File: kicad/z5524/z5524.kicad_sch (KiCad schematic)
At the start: 46 parts, among them J2 Conn_01x01, J3 Conn_02x20_Odd_Even, J4 Conn_01x02, Q2 MMBT3904, U10 LM337L_TO92, U11 PCA9555D, U13 DG442xY, U14 TL072, U19 LM4040BIM3-4.1, U20 M24C02-WMN, U5 LM4040C25FTA, U8 TL074, U9 LM78L05_TO92

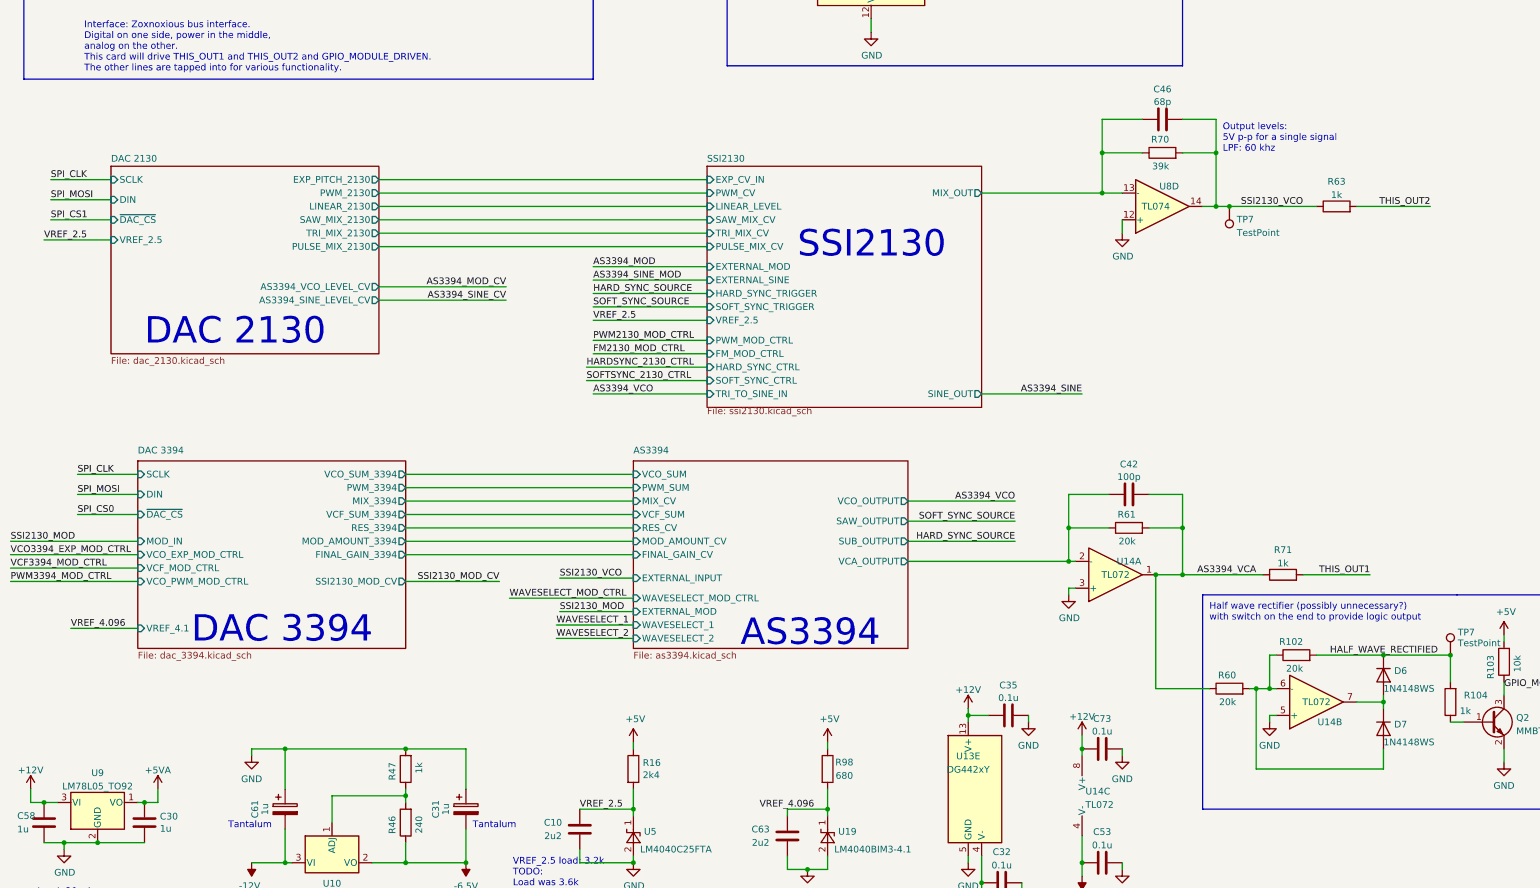
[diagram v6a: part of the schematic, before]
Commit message: updates to scale modulation values better
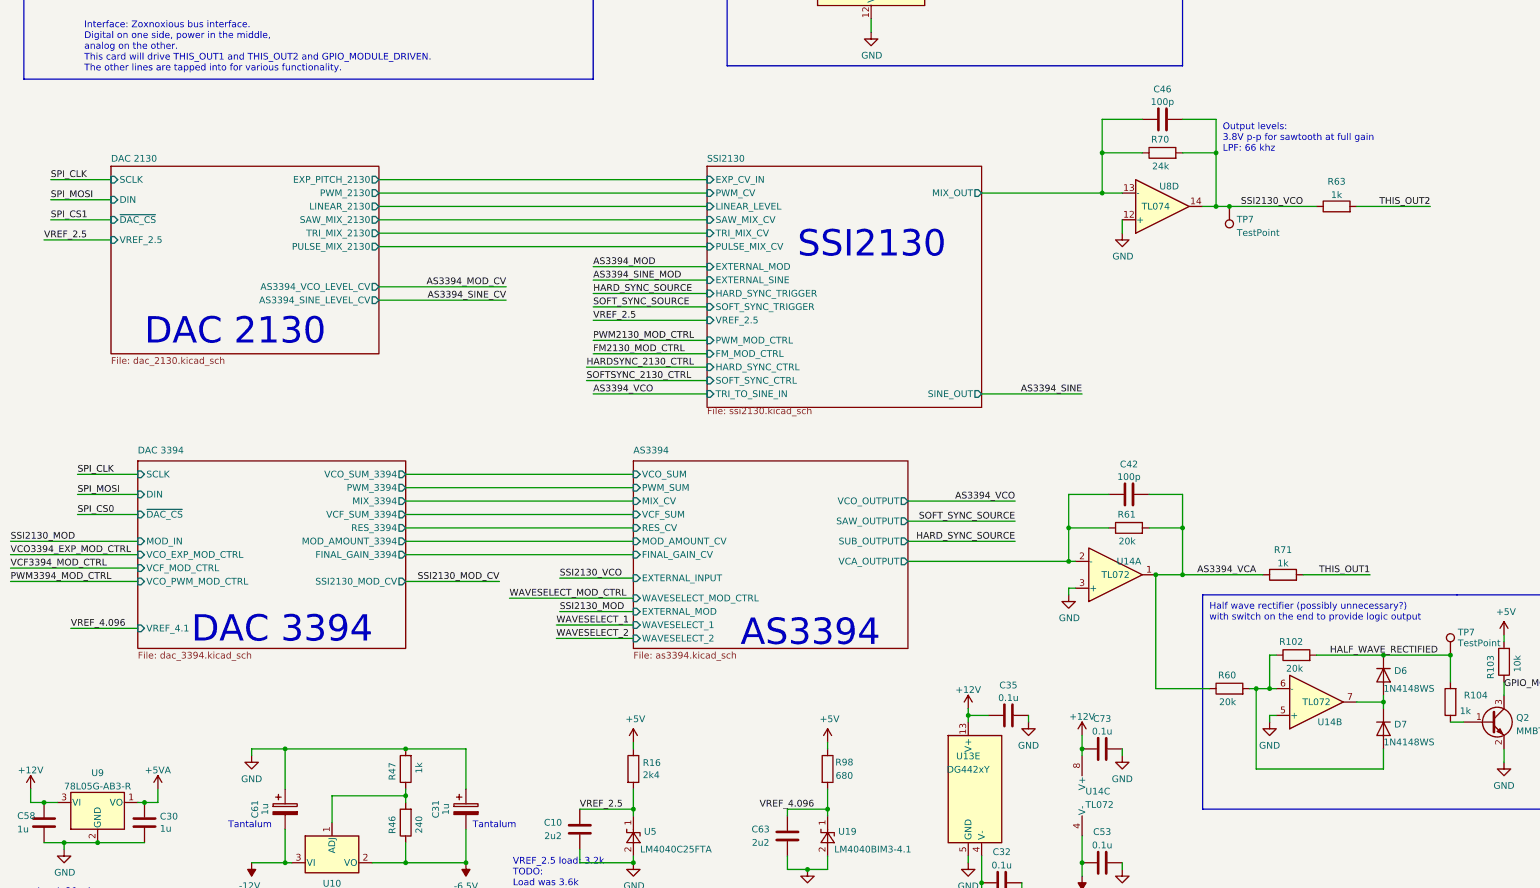
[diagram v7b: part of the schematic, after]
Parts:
- C46: value 68p -> 100p; LCSC C28262 -> C14858
- R70: value 39k -> 24k; LCSC C23153 -> C23352
- U9: value LM78L05_TO92 -> 78L05G-AB3-R; footprint Package_TO_SOT_THT:TO-92_Inline_Wide -> Package_TO_SOT_SMD:SOT-89-3; LCSC (none) -> C71136
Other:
- note added: "Output levels: 3.8V p-p for sawtooth at full gain LPF: 66 khz"
- note removed: "Output levels: 5V p-p for a single signal LPF: 60 khz"
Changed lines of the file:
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@@
     (effects (font (size 1.27 1.27)) (justify left bottom))
   )
-  (text "Output levels:\n5V p-p for a single signal\nLPF: 60 khz"
+  (text "Output levels:\n3.8V p-p for sawtooth at full gain\nLPF: 66 khz"
     (at 243.84 118.11 0)
     (effects (font (size 1.27 1.27)) (justify left bottom))
@@
       (effects (font (size 1.27 1.27)) (justify left))
     )
-    (property "Value" "39k" (at 233.68 120.65 90)
+    (property "Value" "24k" (at 233.68 120.65 90)
       (effects (font (size 1.27 1.27)) (justify left))
     )
@@
       (effects (font (size 1.27 1.27)) hide)
     )
-    (property "LCSC" "C23153" (at 232.41 118.11 0)
+    (property "LCSC" "C23352" (at 232.41 118.11 0)
       (effects (font (size 1.27 1.27)) hide)
     )
@@
       (effects (font (size 1.27 1.27)))
     )
-    (property "Value" "LM78L05_TO92" (at 30.48 238.2321 0)
-      (effects (font (size 1.27 1.27)))
-    )
-    (property "Footprint" "Package_TO_SOT_THT:TO-92_Inline_Wide" (at 30.48 235.585 0)
+    (property "Value" "78L05G-AB3-R" (at 30.48 238.2321 0)
+      (effects (font (size 1.27 1.27)))
+    )
+    (property "Footprint" "Package_TO_SOT_SMD:SOT-89-3" (at 30.48 235.585 0)
       (effects (font (size 1.27 1.27) italic) hide)
     )
-    (property "Datasheet" "https://www.onsemi.com/pub/Collateral/MC78L06A-D.pdf" (at 30.48 242.57 0)
+    (property "Datasheet" "https://datasheet.lcsc.com/lcsc/2304140030_UTC-Unisonic-Tech-78L05G-AB3-R_C71136.pdf" (at 30.48 242.57 0)
+      (effects (font (size 1.27 1.27)) hide)
+    )
+    (property "LCSC" "C71136" (at 30.48 241.3 0)
       (effects (font (size 1.27 1.27)) hide)
     )
@@
       (effects (font (size 1.27 1.27)))
     )
-    (property "Value" "68p" (at 232.41 108.4381 90)
+    (property "Value" "100p" (at 232.41 108.4381 90)
       (effects (font (size 1.27 1.27)))
     )
@@
       (effects (font (size 1.27 1.27)) hide)
     )
-    (property "LCSC" "C28262" (at 232.41 111.76 0)
-      (effects (font (size 1.27 1.27)) hide)
-    )
+    (property "LCSC" "C14858" (at 232.41 111.76 0)
+      (effects (font (size 1.27 1.27)) hide)
+    )

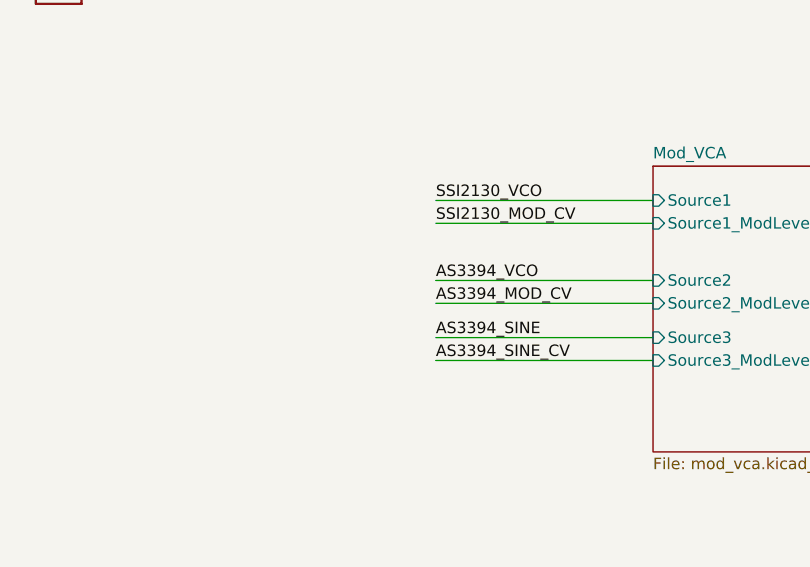
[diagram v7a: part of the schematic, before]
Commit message: schematic updates- cv values from dac and input protections between VCOs
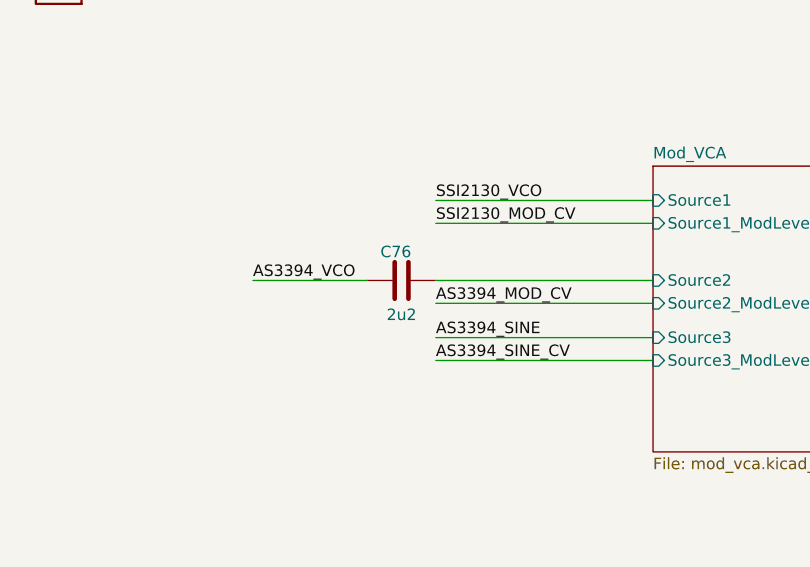
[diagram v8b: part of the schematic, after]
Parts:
- added C76: 2u2, Capacitor_SMD:C_0603_1608Metric, symbol Device:C
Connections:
- net AS3394_VCO: now also C76.2
- new net Mod_VCA/Source2: C76.1
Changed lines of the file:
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@@
+    (stroke (width 0) (type default))
+  )
+  (wire (pts (xy 287.02 160.02) (xy 299.72 160.02))
     (stroke (width 0) (type default))
   )
@@
     (effects (font (size 1.27 1.27)) (justify right bottom))
   )
-  (label "AS3394_VCO" (at 307.34 160.02 0) (fields_autoplaced)
+  (label "AS3394_VCO" (at 287.02 160.02 0) (fields_autoplaced)
     (effects (font (size 1.27 1.27)) (justify left bottom))
   )
@@
         )
       )
+    )
+  )
+  (symbol (lib_id "Device:C") (at 303.53 160.02 270) (unit 1)
+    (in_bom yes) (on_board yes) (dnp no)
+    (property "Reference" "C76" (at 302.895 156.845 90)
+      (effects (font (size 1.27 1.27)))
+    )
+    (property "Value" "2u2" (at 303.53 163.83 90)
+      (effects (font (size 1.27 1.27)))
+    )
+    (property "Footprint" "Capacitor_SMD:C_0603_1608Metric" (at 299.72 160.9852 0)
+      (effects (font (size 1.27 1.27)) hide)
+    )
+    (property "Datasheet" "~" (at 303.53 160.02 0)
+      (effects (font (size 1.27 1.27)) hide)
+    )
+    (property "LCSC" "C23630" (at 303.53 160.02 0)
+      (effects (font (size 1.27 1.27)) hide)
+    )
+    (pin "1")
+    (pin "2")
+    (instances
+      (project "z5524"
+        (path "/7079bdb0-a00e-4bac-b257-cbcf2c91bbd6"
+          (reference "C76") (unit 1)
+        )
+      )
